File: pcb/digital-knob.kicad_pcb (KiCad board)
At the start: 2 copper layers, 70 x 35 mm, 32 parts, among them IC1 ATTINY20-X, P1 CONN_02X02

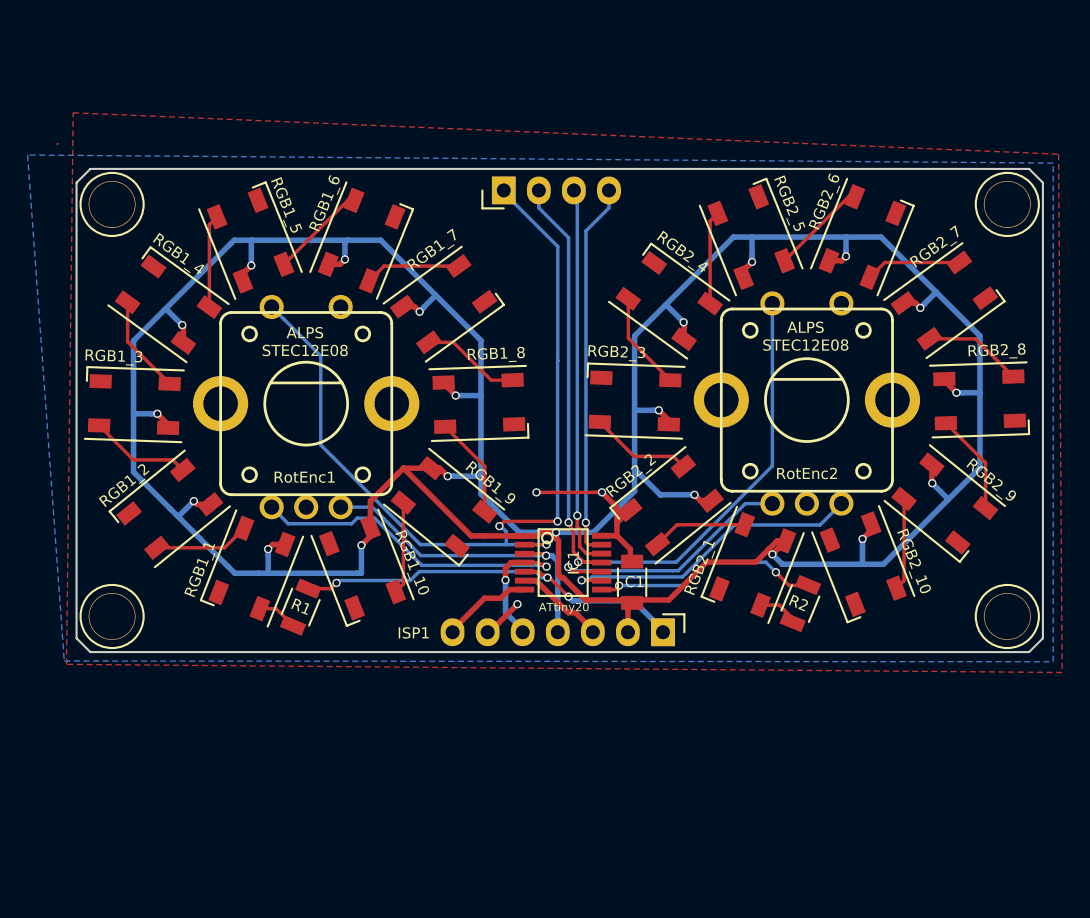
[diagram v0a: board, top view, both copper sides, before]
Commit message: Initial version of v2 single encoder pcb
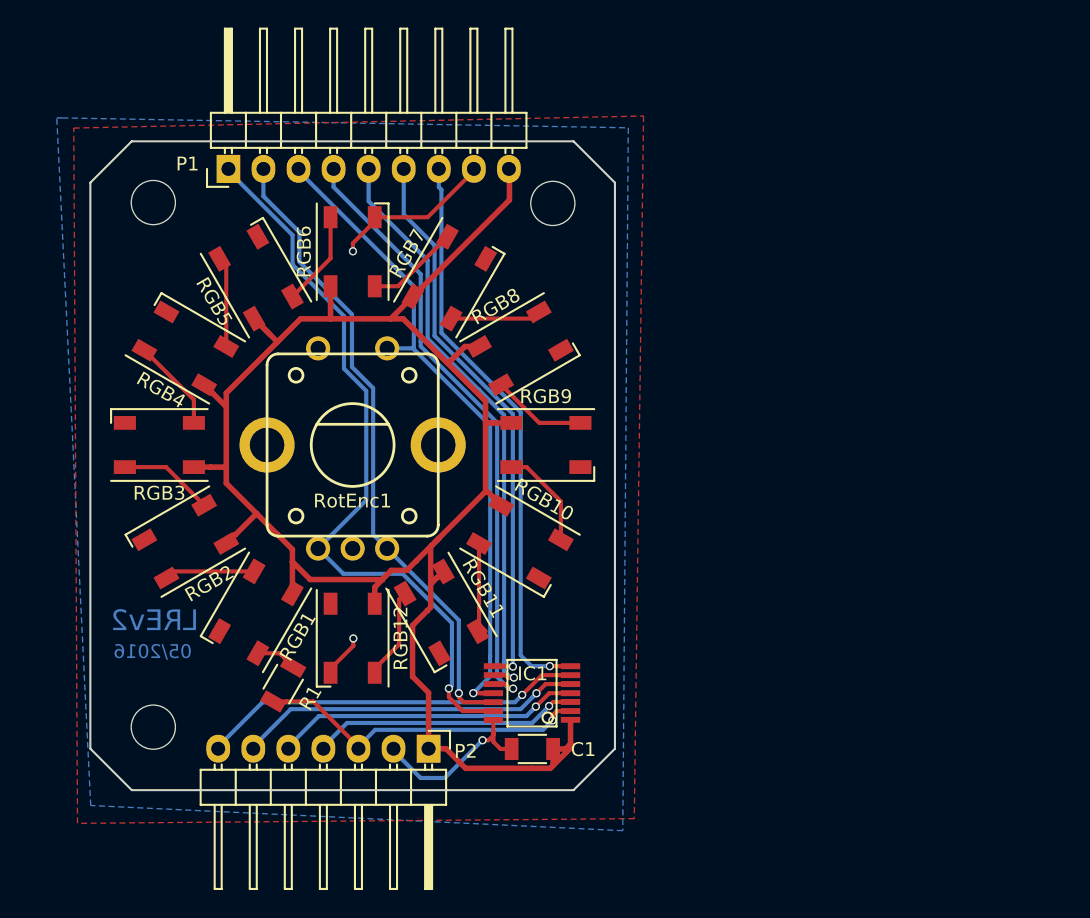
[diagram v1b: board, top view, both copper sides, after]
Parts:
- removed ISP1: CONN_01X07, Pin_Headers:Pin_Header_Angled_1x07
- removed R2: 220Ω, Resistors_SMD:R_1206
- removed REF** (x4): 1pin, Connect:1pin
- removed RGB1_1, RGB1_10, RGB1_2, RGB1_3, RGB1_4, RGB1_5, RGB1_6, RGB1_7, RGB1_8, RGB1_9, RGB2_1, RGB2_10, RGB2_2, RGB2_3, RGB2_4, RGB2_5, RGB2_6, RGB2_7, RGB2_8, RGB2_9: RGB_LED_5050, LEDs:LED_WS2812B-PLCC4
- removed RotEnc2: Rotary_Encoder, Rotary Encoders:ALPS_STEC12E08
- added H1: MountingHole_3.2mm_M3, Mounting_Holes:MountingHole_3.2mm_M3, F.Cu at (85.5, 82.5)
- added H2: MountingHole_3.2mm_M3, Mounting_Holes:MountingHole_3.2mm_M3, F.Cu at (114.5, 82.5)
- added H3: MountingHole_3.2mm_M3, Mounting_Holes:MountingHole_3.2mm_M3, F.Cu at (85.5, 120.5)
- added P2: CONN_01X07, Pin_Headers:Pin_Header_Angled_1x07, F.Cu at (105.5, 122.0)
- added RGB1: RGB_LED_5050, LEDs:LED_WS2812B-PLCC4, F.Cu at (93.0, 112.1)
- added RGB10: RGB_LED_5050, LEDs:LED_WS2812B-PLCC4, F.Cu at (112.1, 107.0)
- added RGB11: RGB_LED_5050, LEDs:LED_WS2812B-PLCC4, F.Cu at (106.4, 112.1)
- added RGB12: RGB_LED_5050, LEDs:LED_WS2812B-PLCC4, F.Cu at (100.0, 114.0)
- added RGB2: RGB_LED_5050, LEDs:LED_WS2812B-PLCC4, F.Cu at (87.9, 107.0)
- added RGB3: RGB_LED_5050, LEDs:LED_WS2812B-PLCC4, F.Cu at (86.0, 100.0)
- added RGB4: RGB_LED_5050, LEDs:LED_WS2812B-PLCC4, F.Cu at (87.9, 93.0)
- added RGB5: RGB_LED_5050, LEDs:LED_WS2812B-PLCC4, F.Cu at (93.0, 87.9)
- added RGB6: RGB_LED_5050, LEDs:LED_WS2812B-PLCC4, F.Cu at (100.0, 86.0)
- added RGB7: RGB_LED_5050, LEDs:LED_WS2812B-PLCC4, F.Cu at (107.0, 87.9)
- added RGB8: RGB_LED_5050, LEDs:LED_WS2812B-PLCC4, F.Cu at (112.1, 93.0)
- added RGB9: RGB_LED_5050, LEDs:LED_WS2812B-PLCC4, F.Cu at (114.0, 100.0)
- P1: value CONN_02X02 -> CONN_01X09; footprint Pin_Headers:Pin_Header_Angled_1x04 -> Pin_Headers:Pin_Header_Angled_1x09
- moved P1 20.0 mm to (91.0, 80.0)
- moved C1 14.1 mm to (113.0, 122.0), turned to 180 degrees
- moved IC1 9.73 mm to (113.0, 118.0), turned to 90 degrees
- moved R1 5.72 mm to (95.0, 117.3), turned to 60 degrees
- moved RotEnc1 4.51 mm to (100.0, 100.0)
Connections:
- P1 pad 2: Net-(IC1-Pad11) -> Net-(IC1-Pad12)
- P1 pad 3: Net-(IC1-Pad12) -> Net-(IC1-Pad11)
- P1 pad 4: Net-(IC1-Pad2) -> Net-(IC1-Pad10)
- R1 pad 1: Net-(IC1-Pad5) -> Net-(IC1-Pad2)
- RotEnc1 pad A: Net-(IC1-Pad4) -> Net-(IC1-Pad13)
- RotEnc1 pad B: Net-(IC1-Pad3) -> Net-(IC1-Pad12)
- RotEnc1 pad SW1: Net-(IC1-Pad2) -> GND
- RotEnc1 pad SW2: GND -> Net-(IC1-Pad11)
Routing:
- net +5V: track 265.6 -> 135.5 mm, vias 21 -> 0
- net Net-(IC1-Pad2): track 63.9 -> 24.5 mm, vias 3 -> 1
- net Net-(IC1-Pad7): track 6.61 -> 41.6 mm, vias 0 -> 1
- net Net-(IC1-Pad13): track 27.4 -> 54.1 mm
- net Net-(IC1-Pad10): track 19.5 -> 44.9 mm
- net Net-(IC1-Pad8): track 16.5 -> 40.8 mm, vias 2 -> 1
- net Net-(IC1-Pad6): track 6.74 -> 27.8 mm, vias 0 -> 1
- net Net-(IC1-Pad9): track 22.6 -> 43.2 mm
- net Net-(IC1-Pad12): track 27.8 -> 46.8 mm
- net GND: track 17.1 -> 28.0 mm
- net Net-(IC1-Pad11): track 58.7 -> 48.6 mm, vias 2 -> 1
- net Net-(IC1-Pad4): track 30.8 -> 22.4 mm, vias 2 -> 1
- net Net-(RGB10-Pad4): track 0.00 -> 7.39 mm
- net Net-(RGB2_2-Pad2): track 7.39 -> 0.00 mm
- net Net-(RGB1_2-Pad2): track 7.39 -> 0.00 mm
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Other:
- board size 70 x 35 mm -> 38 x 47 mm
- net class 5V added: clearance 0.2, trace_width 0.4, via_dia 0.8, via_drill 0.6
- net class Default: trace_width 0.25 -> 0.3
- rule trace_min: 0.2 -> 0.3
- board text added: "05/2016"
- board text added: "LREv2"
- board text removed: "ALPS STEC12E08"
- board text removed: "ATtiny20"
